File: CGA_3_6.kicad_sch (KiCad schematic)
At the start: 21 parts, among them U1 74S112, U11 74LS74, U12 74LS393, U13 74LS08, U15 74LS00, U16 74LS04, U17 74LS138, U18 74LS138, U19 74LS138, U26 74S04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

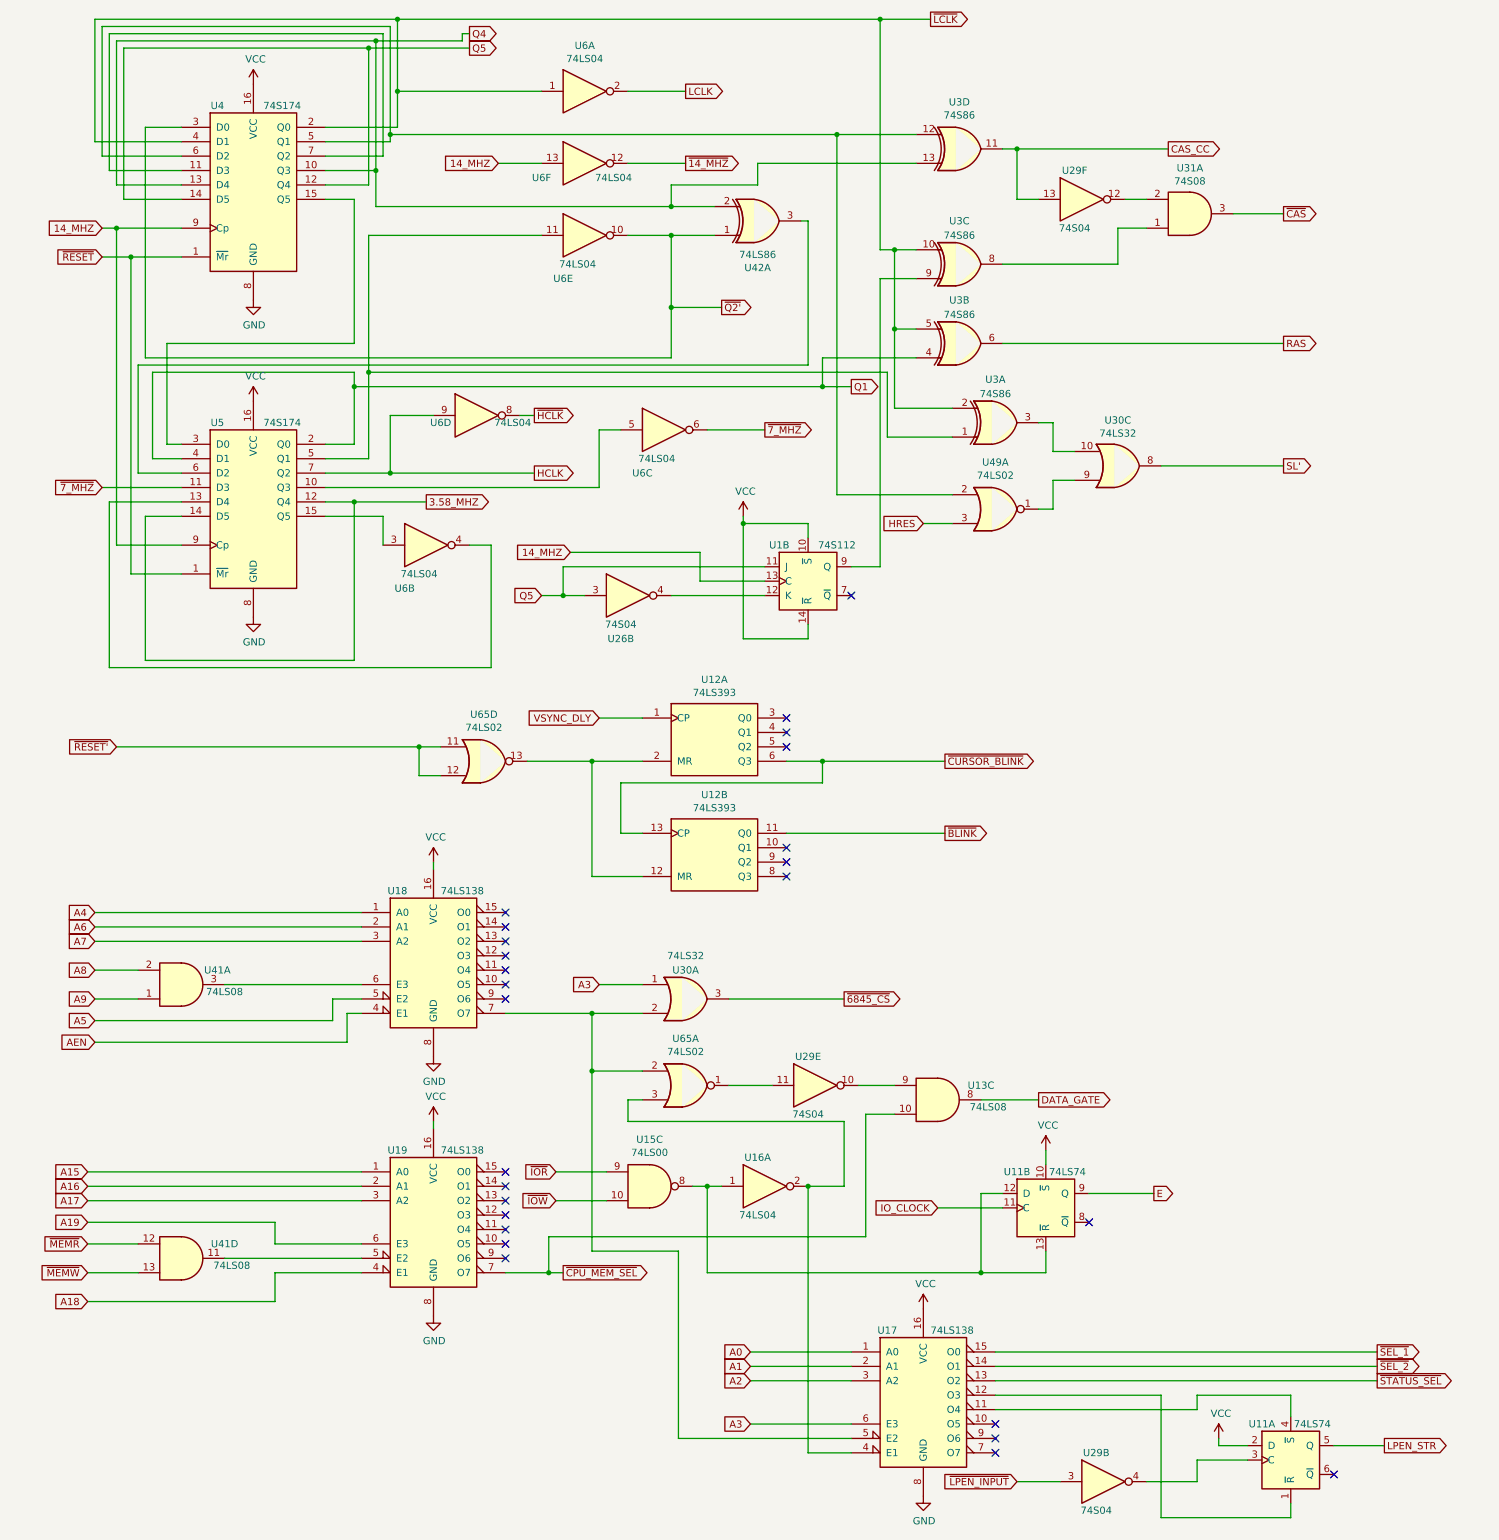
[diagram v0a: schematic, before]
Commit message: Fix Q1' naming thanks to Michael Karcher
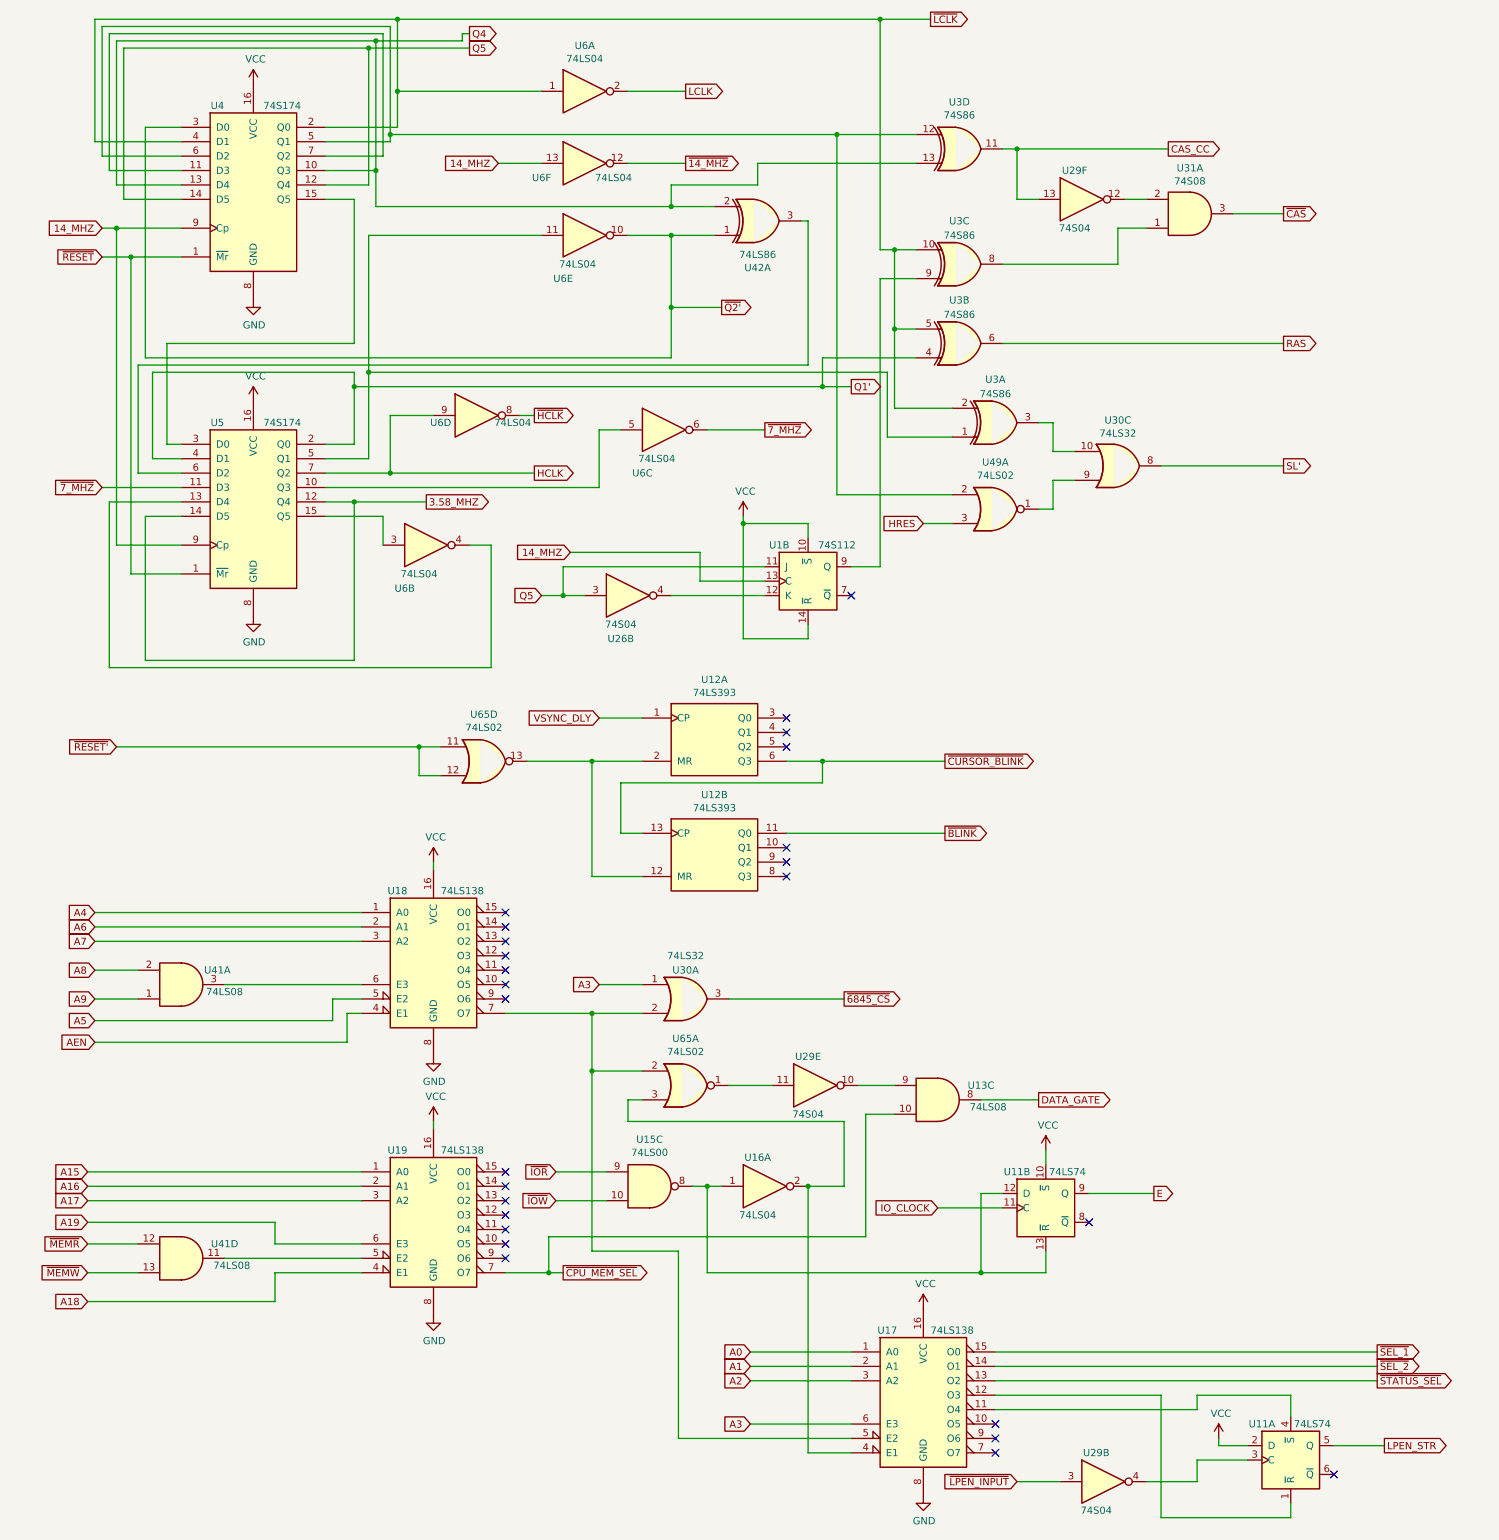
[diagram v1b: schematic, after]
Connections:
- net Q1 renamed Q1'
